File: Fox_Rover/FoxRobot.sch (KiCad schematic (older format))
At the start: 33 parts, among them J1 Screw_Terminal_01x02, J2 XT60-M_Green, J3 XT60-M_Red, J4 Screw_Terminal_01x02, J5 Conn_02x10_Odd_Even, J6 Screw_Terminal_01x02, K1 40.52.7.012.0000, K2 G2RK-1_12DC, K3 ADJH23005, K4 ADJH23005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

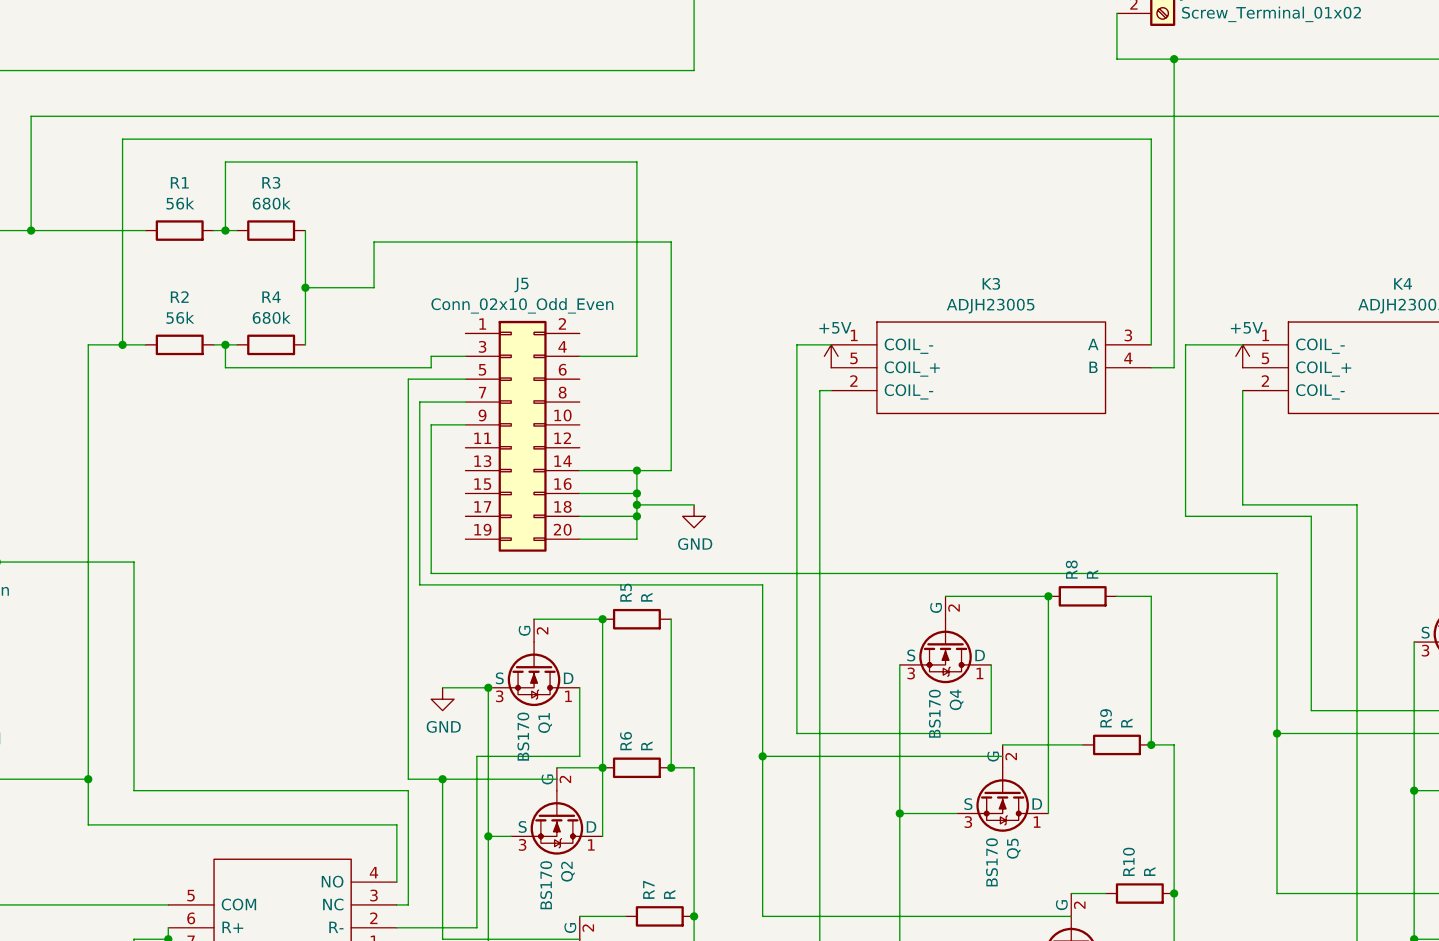
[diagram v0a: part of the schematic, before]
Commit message: Added an extra header output to the schematics and started initial PCB designs
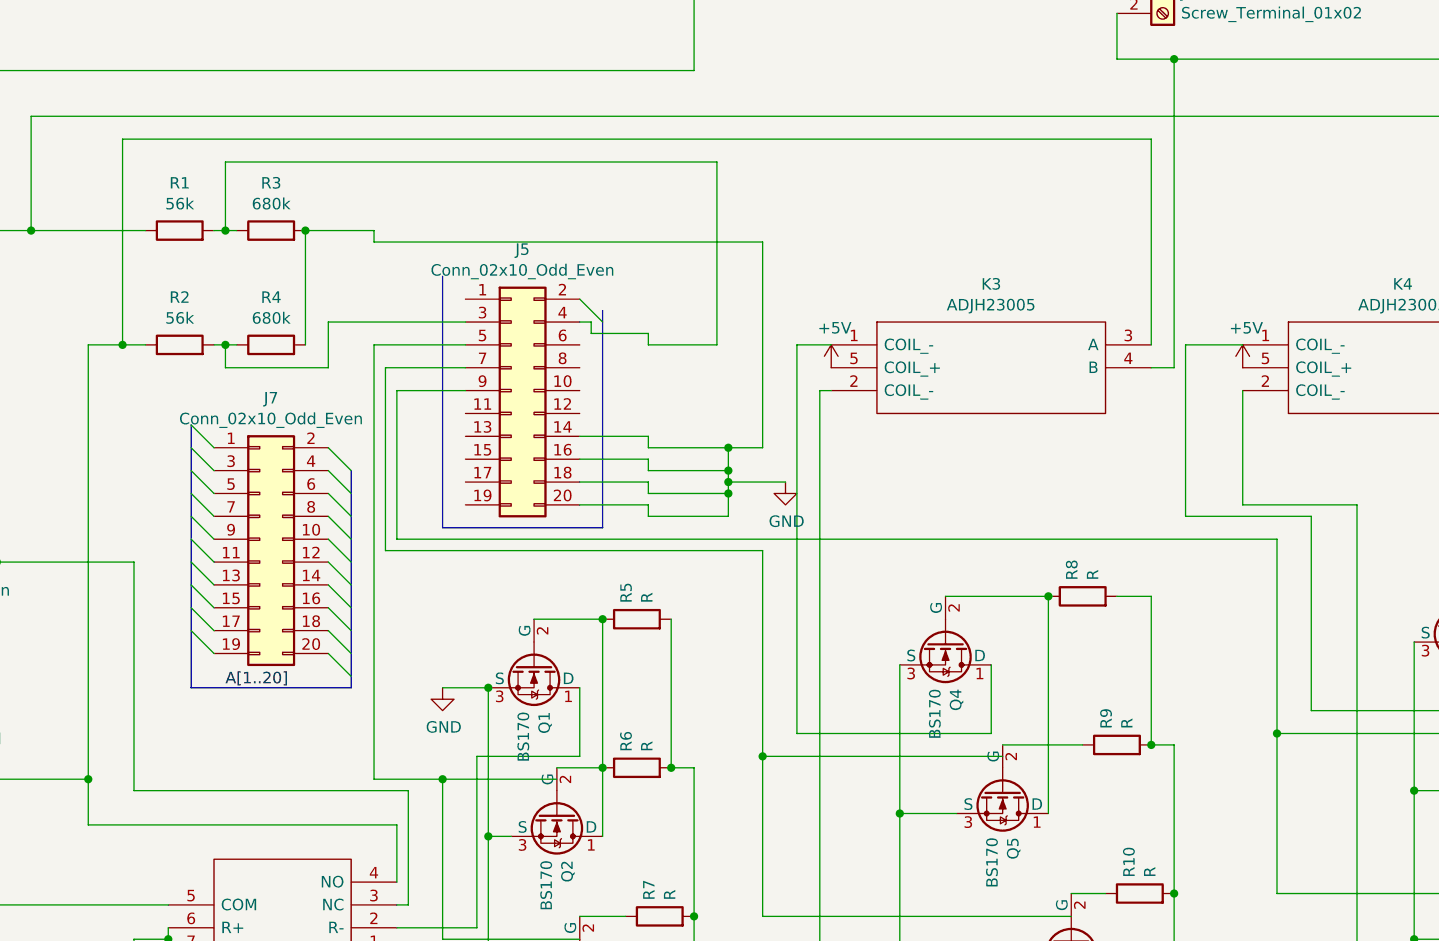
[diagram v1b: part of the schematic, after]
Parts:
- added J7: Conn_02x10_Odd_Even, Connector_PinSocket_2.54mm:PinSocket_2x10_P2.54mm_Vertical, symbol Connector_Generic:Conn_02x10_Odd_Even
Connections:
- net labels added: A[1..20]
- wire segments 196 -> 207
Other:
- moved on the sheet: J5
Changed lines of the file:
@@
 L Connector_Generic:Conn_02x10_Odd_Even J5
 U 1 1 61824C6C
-P 4150 2850
-F 0 "J5" H 4200 3467 50  0000 C CNN
-F 1 "Conn_02x10_Odd_Even" H 4200 3376 50  0000 C CNN
-F 2 "Connector_PinSocket_2.54mm:PinSocket_2x10_P2.54mm_Vertical" H 4150 2850 50  0001 C CNN
-F 3 "~" H 4150 2850 50  0001 C CNN
-	1    4150 2850
+P 4150 2700
+F 0 "J5" H 4200 3317 50  0000 C CNN
+F 1 "Conn_02x10_Odd_Even" H 4200 3226 50  0000 C CNN
+F 2 "Connector_PinSocket_2.54mm:PinSocket_2x10_P2.54mm_Vertical" H 4150 2700 50  0001 C CNN
+F 3 "~" H 4150 2700 50  0001 C CNN
+	1    4150 2700
 	1    0    0    -1
 $EndComp
@@
 Wire Wire Line
 	2900 2500 2900 2600
-Wire Wire Line
-	3800 2600 3800 2550
-Wire Wire Line
-	3800 2550 3950 2550
 Connection ~ 2900 2500
 Wire Wire Line
 	2900 2500 2950 2500
 Wire Wire Line
-	2900 1700 4700 1700
-Wire Wire Line
-	4700 2550 4450 2550
+	2900 1700 5050 1700
 Connection ~ 2900 2000
 Wire Wire Line
 	2900 2000 2950 2000
-Wire Wire Line
-	4450 3050 4700 3050
-Wire Wire Line
-	4700 3050 4700 3150
-Wire Wire Line
-	4700 3350 4450 3350
-Wire Wire Line
-	4450 3250 4700 3250
-Connection ~ 4700 3250
-Wire Wire Line
-	4700 3250 4700 3350
-Wire Wire Line
-	4450 3150 4700 3150
-Connection ~ 4700 3150
-Wire Wire Line
-	4700 3150 4700 3200
 $Comp
 L power:GND #PWR01
 U 1 1 6183ED9D
-P 4950 3200
-F 0 "#PWR01" H 4950 2950 50  0001 C CNN
-F 1 "GND" H 4955 3027 50  0000 C CNN
-F 2 "" H 4950 3200 50  0001 C CNN
-F 3 "" H 4950 3200 50  0001 C CNN
-	1    4950 3200
-	1    0    0    -1
-$EndComp
-Wire Wire Line
-	4700 3200 4950 3200
-Connection ~ 4700 3200
-Wire Wire Line
-	4700 3200 4700 3250
-Wire Wire Line
-	3250 2500 3250 2250
-Wire Wire Line
-	3250 2250 3550 2250
-Wire Wire Line
-	3550 2250 3550 2050
-Wire Wire Line
-	3550 2050 4850 2050
-Connection ~ 3250 2250
-Wire Wire Line
-	3250 2250 3250 2000
+P 5350 3100
+F 0 "#PWR01" H 5350 2850 50  0001 C CNN
+F 1 "GND" H 5355 2927 50  0000 C CNN
+F 2 "" H 5350 3100 50  0001 C CNN
+F 3 "" H 5350 3100 50  0001 C CNN
+	1    5350 3100
+	1    0    0    -1
+$EndComp
+Wire Wire Line
+	5100 3100 5350 3100
+Connection ~ 5100 3100
+Wire Wire Line
+	3250 2500 3250 2000
+Wire Wire Line
+	3250 2000 3550 2000
+Wire Wire Line
+	3550 2000 3550 2050
+Connection ~ 3250 2000
 Wire Wire Line
 	2900 1700 2900 2000
-Wire Wire Line
-	4700 1700 4700 2550
 $Comp
 L Transistor_FET:BS170 Q1
@@
 	2650 5100 2650 5150
 Wire Wire Line
-	2900 2600 3800 2600
-Wire Wire Line
 	4350 4400 3850 4400
 Wire Wire Line
@@
 Connection ~ 3850 4400
 Wire Wire Line
-	3850 4400 3700 4400
-Wire Wire Line
 	2450 5450 2450 6000
 Connection ~ 2450 5450
@@
 Connection ~ 850  4100
 Wire Wire Line
-	3700 2650 3700 4400
-Wire Wire Line
-	3700 2650 3950 2650
-Wire Wire Line
-	3950 2750 3750 2750
-Wire Wire Line
-	3750 2750 3750 3550
-Wire Wire Line
-	3750 3550 5250 3550
+	3600 3400 5250 3400
 $Comp
 L Transistor_FET:BS170 Q4
@@
 Connection ~ 5250 4300
 Wire Wire Line
-	5250 3550 5250 4300
+	5250 3400 5250 4300
 Wire Wire Line
 	5250 4300 5250 5000
@@
 	7500 4900 7500 4200
 Wire Wire Line
-	7500 4200 7500 3500
-Wire Wire Line
-	7500 3500 3800 3500
-Wire Wire Line
-	3800 3500 3800 2850
-Wire Wire Line
-	3800 2850 3950 2850
+	7500 4200 7500 3350
+Wire Wire Line
+	7500 3350 3650 3350
 Connection ~ 7500 4200
 Wire Wire Line
@@
 NoConn ~ 2000 5650
 Wire Wire Line
-	4850 2050 4850 3050
-Wire Wire Line
-	4850 3050 4700 3050
-Connection ~ 4700 3050
+	5250 2950 5100 2950
 Wire Wire Line
 	4950 1300 850  1300
@@
 	2200 5450 2450 5450
 $Comp
-L power:+5V #PWR?
+L power:+5V #PWR02
 U 1 1 61BB12DC
 P 5550 2600
-F 0 "#PWR?" H 5550 2450 50  0001 C CNN
+F 0 "#PWR02" H 5550 2450 50  0001 C CNN
 F 1 "+5V" H 5565 2773 50  0000 C CNN
 F 2 "" H 5550 2600 50  0001 C CNN
@@
 $EndComp
 $Comp
-L power:+5V #PWR?
+L power:+5V #PWR03
 U 1 1 61BB1EDB
 P 7350 2600
-F 0 "#PWR?" H 7350 2450 50  0001 C CNN
+F 0 "#PWR03" H 7350 2450 50  0001 C CNN
 F 1 "+5V" H 7365 2773 50  0000 C CNN
 F 2 "" H 7350 2600 50  0001 C CNN
@@
 	1    0    0    -1
 $EndComp
+Wire Wire Line
+	3650 3350 3650 2700
+Wire Wire Line
+	3600 2600 3600 3400
+Wire Wire Line
+	2900 2600 3350 2600
+Wire Wire Line
+	3350 2600 3350 2400
+Wire Wire Line
+	5050 1700 5050 2500
+Wire Wire Line
+	5100 3100 5100 3150
+Wire Wire Line
+	5100 3150 5100 3250
+Connection ~ 5100 3150
+Wire Wire Line
+	5100 3050 5100 3100
+Wire Wire Line
+	5100 2950 5100 3050
+Connection ~ 5100 3050
+Connection ~ 5100 2950
+Wire Wire Line
+	3350 2400 3950 2400
+Wire Wire Line
+	3950 2600 3600 2600
+Wire Wire Line
+	3650 2700 3950 2700
+Wire Wire Line
+	5100 3250 4750 3250
+Wire Wire Line
+	4750 3150 5100 3150
+Wire Wire Line
+	4750 3050 5100 3050
+Wire Wire Line
+	4750 2950 5100 2950
+Wire Wire Line
+	3850 4400 3550 4400
+Wire Wire Line
+	3550 2500 3950 2500
+Wire Wire Line
+	3550 2500 3550 4400
+$Comp
+L Connector_Generic:Conn_02x10_Odd_Even J7
+U 1 1 618C4DF2
+P 3050 3350
+F 0 "J7" H 3100 3967 50  0000 C CNN
+F 1 "Conn_02x10_Odd_Even" H 3100 3876 50  0000 C CNN
+F 2 "Connector_PinSocket_2.54mm:PinSocket_2x10_P2.54mm_Vertical" H 3050 3350 50  0001 C CNN
+F 3 "~" H 3050 3350 50  0001 C CNN
+	1    3050 3350
+	1    0    0    -1
+$EndComp
+Wire Bus Line
+	2750 4000 3450 4000
+Entry Wire Line
+	3350 2950 3450 3050
+Entry Wire Line
+	3350 3050 3450 3150
+Entry Wire Line
+	3350 3150 3450 3250
+Entry Wire Line
+	3350 3250 3450 3350
+Entry Wire Line
+	3350 3350 3450 3450
+Entry Wire Line
+	3350 3450 3450 3550
+Entry Wire Line
+	3350 3550 3450 3650
+Entry Wire Line
+	3350 3650 3450 3750
+Entry Wire Line
+	3350 3750 3450 3850
+Entry Wire Line
+	3350 3850 3450 3950
+Entry Wire Line
+	2750 2850 2850 2950
+Entry Wire Line
+	2750 2950 2850 3050
+Entry Wire Line
+	2750 3050 2850 3150
+Entry Wire Line
+	2750 3150 2850 3250
+Entry Wire Line
+	2750 3250 2850 3350
+Entry Wire Line
+	2750 3350 2850 3450
+Entry Wire Line
+	2750 3450 2850 3550
+Entry Wire Line
+	2750 3550 2850 3650
+Entry Wire Line
+	2750 3650 2850 3750
+Entry Wire Line
+	2750 3750 2850 3850
+Text Label 2900 4000 0    50   ~ 0
+A[1..20]
+Wire Wire Line
+	4450 2900 4750 2900
+Wire Wire Line
+	4750 2900 4750 2950
+Wire Wire Line
+	4450 3000 4750 3000
+Wire Wire Line
+	4750 3000 4750 3050
+Wire Wire Line
+	4450 3100 4750 3100
+Wire Wire Line
+	4750 3100 4750 3150
+Wire Wire Line
+	4450 3200 4750 3200
+Wire Wire Line
+	4750 3200 4750 3250
+Wire Wire Line
+	3550 2050 5250 2050
+Wire Wire Line
+	5250 2050 5250 2950
+Wire Wire Line
+	4750 2500 5050 2500
+Wire Bus Line
+	4550 3300 3850 3300
+Wire Bus Line
+	3850 3300 3850 2200
+Entry Wire Line
+	4450 2300 4550 2400
+Wire Wire Line
+	4500 2400 4500 2450
+Wire Wire Line
+	4500 2450 4750 2450
+Wire Bus Line
+	4550 2350 4550 3300
+Wire Wire Line
+	4450 2400 4500 2400
+Wire Bus Line
+	2750 2850 2750 4000
+Wire Bus Line
+	3450 3050 3450 4000
+Wire Wire Line
+	4750 2450 4750 2500
 $EndSCHEMATC

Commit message: PCB design suitable
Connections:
- net labels added: A1, A10, A11, A12, A13, A14, A15, A16, A17, A18, A19, A2, A20, A3, A4, A5, A6, A7, A8, A9
- net labels removed: A[1..20]
- wire segments 207 -> 236
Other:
- moved on the sheet: J7

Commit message: Adjusted for mounting platforms
Adjust sizing for lower pricing
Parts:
- added H1, H2, H3, H4: MountingHole, MountingHole:MountingHole_3.2mm_M3_ISO7380_Pad_TopBottom, symbol Mechanical:MountingHole
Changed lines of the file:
@@
 Wire Wire Line
 	3700 3200 3950 3200
+$Comp
+L Mechanical:MountingHole H1
+U 1 1 621F6ABB
+P 1150 1550
+F 0 "H1" H 1250 1596 50  0000 L CNN
+F 1 "MountingHole" H 1250 1505 50  0000 L CNN
+F 2 "MountingHole:MountingHole_3.2mm_M3_ISO7380_Pad_TopBottom" H 1150 1550 50  0001 C CNN
+F 3 "~" H 1150 1550 50  0001 C CNN
+	1    1150 1550
+	1    0    0    -1
+$EndComp
+$Comp
+L Mechanical:MountingHole H2
+U 1 1 621F8225
+P 1150 1750
+F 0 "H2" H 1250 1796 50  0000 L CNN
+F 1 "MountingHole" H 1250 1705 50  0000 L CNN
+F 2 "MountingHole:MountingHole_3.2mm_M3_ISO7380_Pad_TopBottom" H 1150 1750 50  0001 C CNN
+F 3 "~" H 1150 1750 50  0001 C CNN
+	1    1150 1750
+	1    0    0    -1
+$EndComp
+$Comp
+L Mechanical:MountingHole H3
+U 1 1 622083F5
+P 1150 1900
+F 0 "H3" H 1250 1946 50  0000 L CNN
+F 1 "MountingHole" H 1250 1855 50  0000 L CNN
+F 2 "MountingHole:MountingHole_3.2mm_M3_ISO7380_Pad_TopBottom" H 1150 1900 50  0001 C CNN
+F 3 "~" H 1150 1900 50  0001 C CNN
+	1    1150 1900
+	1    0    0    -1
+$EndComp
+$Comp
+L Mechanical:MountingHole H4
+U 1 1 62218B14
+P 1150 2100
+F 0 "H4" H 1250 2146 50  0000 L CNN
+F 1 "MountingHole" H 1250 2055 50  0000 L CNN
+F 2 "MountingHole:MountingHole_3.2mm_M3_ISO7380_Pad_TopBottom" H 1150 2100 50  0001 C CNN
+F 3 "~" H 1150 2100 50  0001 C CNN
+	1    1150 2100
+	1    0    0    -1
+$EndComp
 $EndSCHEMATC

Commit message: Added the filter capacitor and coil.
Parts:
- added C1: 330uF, Capacitor_THT:C_Disc_D7.5mm_W2.5mm_P5.00mm, symbol Device:C
- added C2: 100uF, Capacitor_THT:C_Disc_D7.5mm_W2.5mm_P5.00mm, symbol Device:C
- added L1: L, Inductor_THT:L_Radial_D10.0mm_P5.00mm_Fastron_07M, symbol Device:L
- R10, R11, R12, R13, R5, R6, R7, R8, R9: value R -> 10k
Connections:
- wire segments 236 -> 246
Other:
- moved on the sheet: H1, H2, H3, H4, J2, J3, J5, J6, J7, K2, K3, K4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

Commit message: Adjusted libraries pathing
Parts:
- K3: value ADJH23005 -> POWER_RELAY_RED
- K4: value ADJH23005 -> POWER_RELAY_GREEN
- renumbered K2 to LOGIC_RELAY1
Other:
- note added: "/**** RELAY PINS ****/\n LOGIC_RELAY_BAT_GREEN = PC_2, // EXT_PIN9\n LOGIC_RELAY_BAT_RED = PC_3, // EXT_PIN10\n POWER_RELAY_GREEN_ON = PC_0, // EXT_PIN5\n POWER_RELAY_GREEN_OFF = PD_6, // EXT_PIN6\n POWER_RELAY_RED_ON = PD_5, // EXT_PIN7\n POWER_RELAY_RED_OFF = PB_13, // EXT_PIN8"
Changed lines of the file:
@@
 Connection ~ 5850 4050
 $Comp
-L SamacSys_Parts:G2RK-1_12DC K2
+L SamacSys_Parts:G2RK-1_12DC LOGIC_RELAY1
 U 1 1 618479C8
 P 4550 4850
-F 0 "K2" H 5050 5115 50  0000 C CNN
+F 0 "LOGIC_RELAY1" H 5050 5115 50  0000 C CNN
 F 1 "G2RK-1_12DC" H 5050 5024 50  0000 C CNN
 F 2 "SamacSys_Parts:G2RK112DC" H 5400 4950 50  0001 L CNN
@@
 P 6450 2200
 F 0 "K3" H 7150 2465 50  0000 C CNN
-F 1 "ADJH23005" H 7150 2374 50  0000 C CNN
+F 1 "POWER_RELAY_RED" H 7150 2374 50  0000 C CNN
 F 2 "SamacSys_Parts:ADJH23005" H 7700 2300 50  0001 L CNN
 F 3 "https://industrial.panasonic.com/ac/cdn/e/control/relay/power/catalog/mech_eng_djh.pdf" H 7700 2200 50  0001 L CNN
@@
 P 8250 2200
 F 0 "K4" H 8950 2465 50  0000 C CNN
-F 1 "ADJH23005" H 8950 2374 50  0000 C CNN
+F 1 "POWER_RELAY_GREEN" H 8950 2374 50  0000 C CNN
 F 2 "SamacSys_Parts:ADJH23005" H 9500 2300 50  0001 L CNN
 F 3 "https://industrial.panasonic.com/ac/cdn/e/control/relay/power/catalog/mech_eng_djh.pdf" H 9500 2200 50  0001 L CNN
@@
 Wire Wire Line
 	5450 3400 5550 3400
+Text Notes 4550 6700 0    50   ~ 0
+    /**** RELAY PINS ****/\n    LOGIC_RELAY_BAT_GREEN = PC_2,   // EXT_PIN9\n    LOGIC_RELAY_BAT_RED = PC_3,     // EXT_PIN10\n    POWER_RELAY_GREEN_ON = PC_0,    // EXT_PIN5\n    POWER_RELAY_GREEN_OFF = PD_6,   // EXT_PIN6\n    POWER_RELAY_RED_ON = PD_5,      // EXT_PIN7\n    POWER_RELAY_RED_OFF = PB_13,    // EXT_PIN8
 $EndSCHEMATC
